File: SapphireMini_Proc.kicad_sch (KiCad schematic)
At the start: 38 parts, among them J801 USB_B_Micro, J802 Conn_02x05_Odd_Even, J803 Conn_02x05_Odd_Even, J805 Conn_01x04_Male, SW701 EVQP7C01P, SW801 EVQP7C01P, U801 ATSAMD21G18A-A

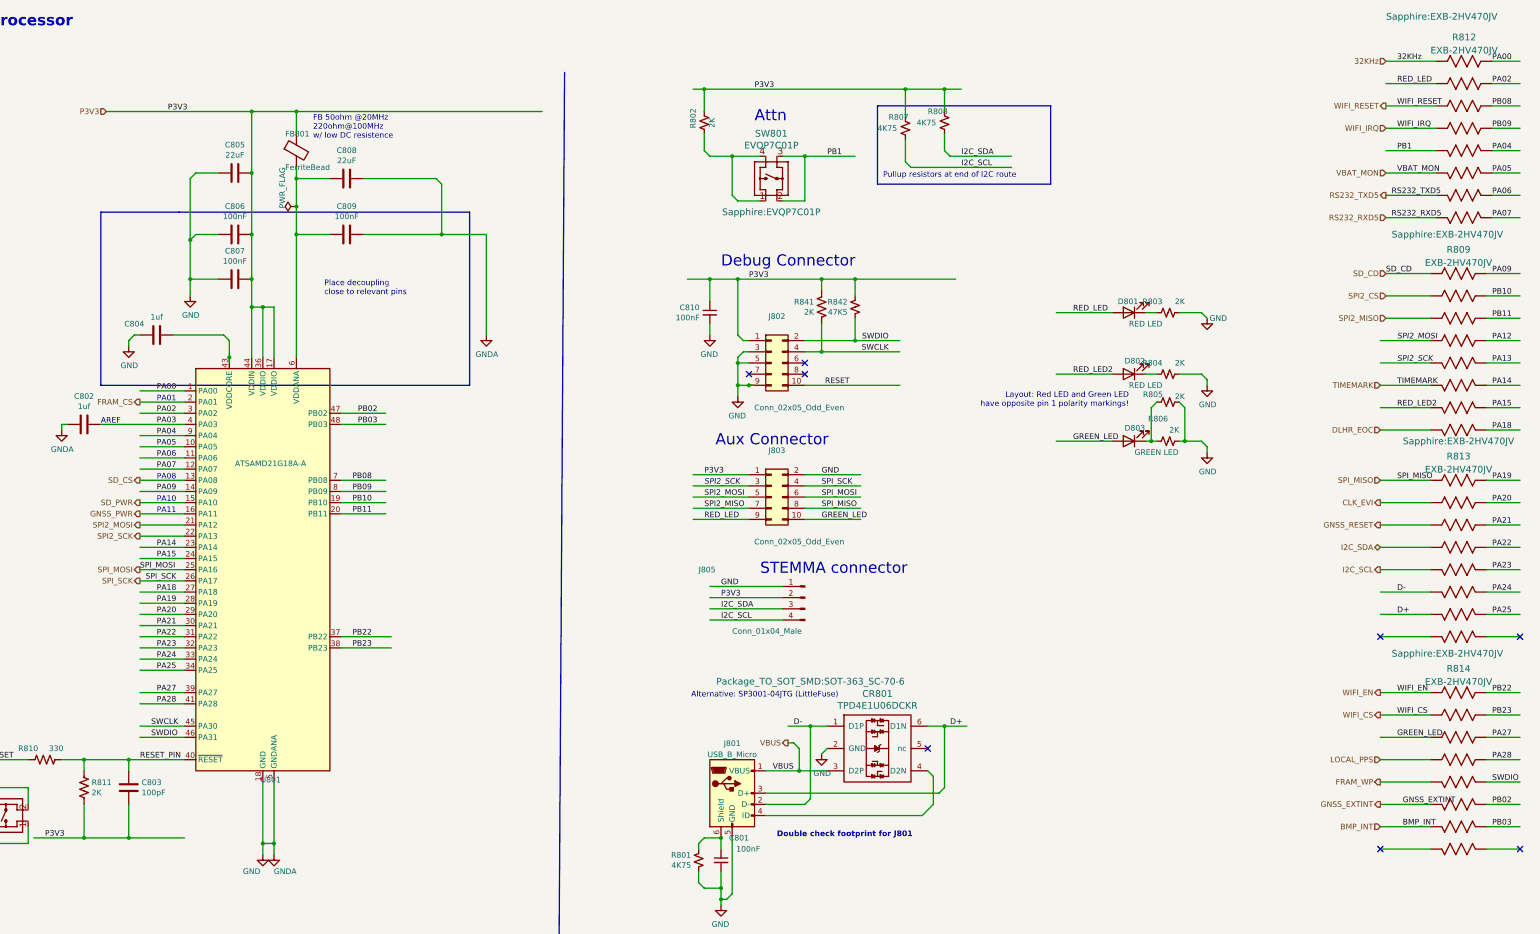
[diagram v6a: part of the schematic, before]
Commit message: 6 Layer Routing
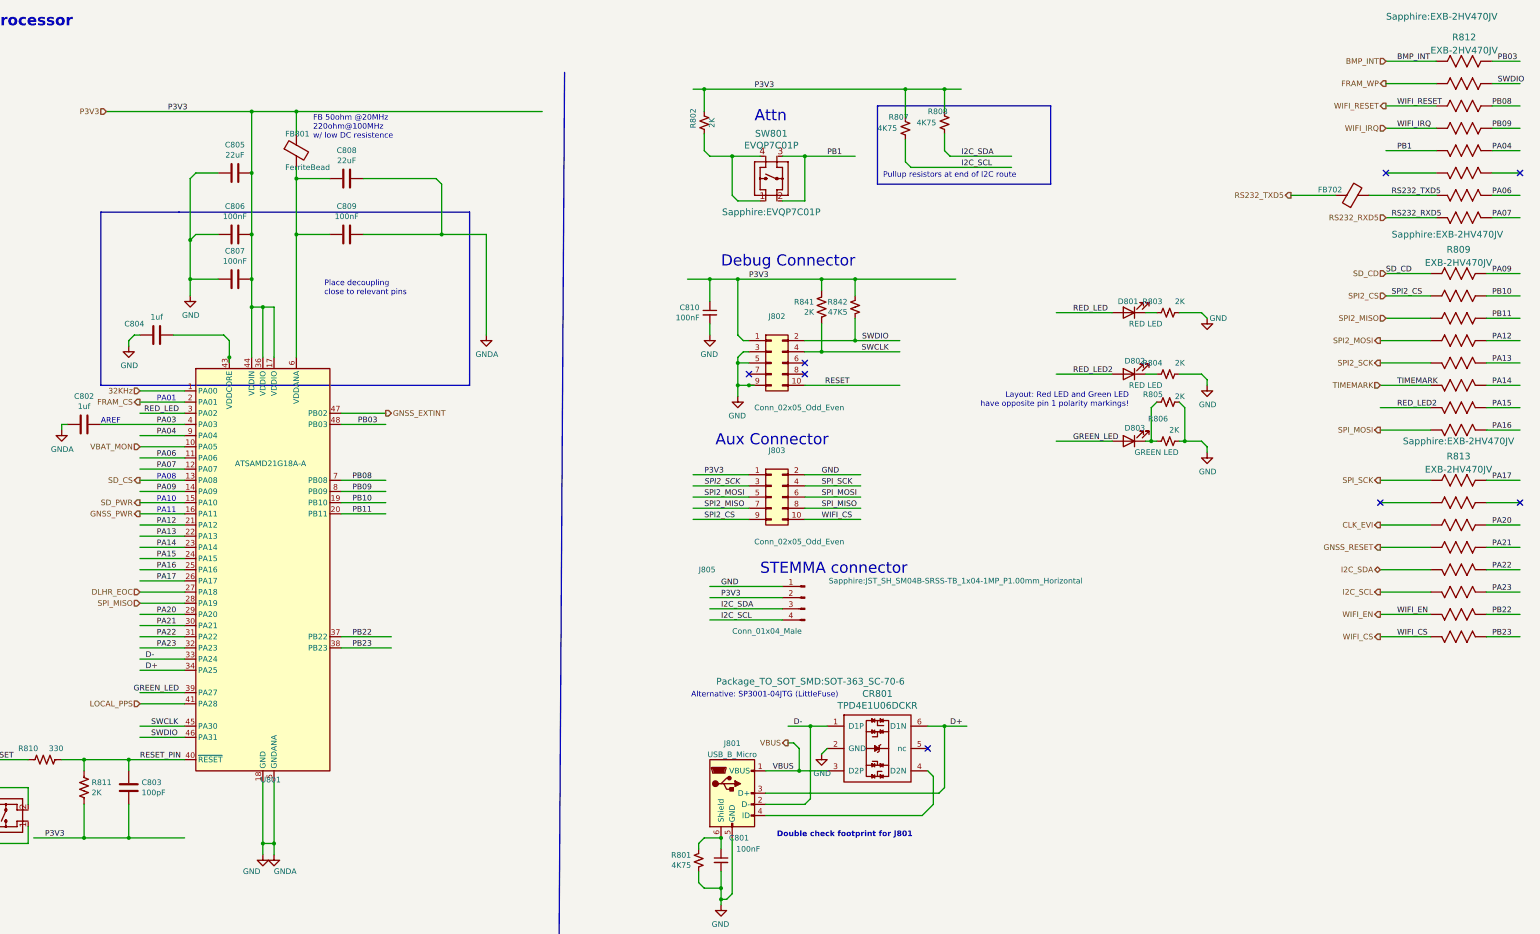
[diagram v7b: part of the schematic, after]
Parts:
- removed R814: EXB-2HV470JV, Sapphire:EXB-2HV470JV, symbol sapphireMini:EXB-2HV470JV_1
- added FB702: FerriteBead, Inductor_SMD:L_0603_1608Metric, symbol Device:FerriteBead
- FB801: footprint Inductor_SMD:L_0201_0603Metric -> Inductor_SMD:L_0603_1608Metric
- J805: footprint Connector_JST:JST_SH_SM04B-SRSS-TB_1x04-1MP_P1.00mm_Horizontal -> Sapphire:JST_SH_SM04B-SRSS-TB_1x04-1MP_P1.00mm_Horizontal; symbol Connector:Conn_01x04_Male -> sapphireMini:Conn_01x04_Male
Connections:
- net PA27 is gone; now on net GREEN_LED: U801.39 (PA27)
- net PA28 is gone; now on net LOCAL_PPS: U801.41 (PA28)
- net PB02 is gone; now on net GNSS_EXTINT: U801.47 (PB02)
- net 32KHz: now also U801.1 (PA00); no longer R812.1
- net BMP_INT: now also R812.1
- net CLK_EVI: now also R813.3; no longer R813.2
- net D+: now also U801.34 (PA25); no longer R813.7
- net D-: now also U801.33 (PA24); no longer R813.6
- net DLHR_EOC: now also U801.27 (PA18); no longer R809.8
- net FRAM_WP: now also R812.2
- net GNSS_RESET: now also R813.4; no longer R813.3
- net GREEN_LED: no longer J803.10 (Pin_10)
- net I2C_SCL: now also R813.6; no longer R813.5
- net I2C_SDA: now also R813.5; no longer R813.4
- net PA12: now also U801.21 (PA12)
- net PA13: now also U801.22 (PA13)
- net PA20: now also R813.14; no longer R813.15
- net PA21: now also R813.13; no longer R813.14
- net PA22: now also R813.12; no longer R813.13
- net PA23: now also R813.11; no longer R813.12
- net PB03: now also R812.16
- net PB22: now also R813.10
- net PB23: now also R813.9
- net RED_LED: now also U801.3 (PA02); no longer J803.9 (Pin_9), R812.2
- net RS232_TXD5: now also FB702.1, FB702.2
- net SPI2_CS: now also J803.9 (Pin_9)
- net SPI2_MOSI: no longer U801.21 (PA12)
- net SPI2_SCK: no longer U801.22 (PA13)
- net SPI_MISO: now also U801.28 (PA19); no longer R813.1
- net SPI_MOSI: now also R809.8; no longer U801.25 (PA16)
- net SPI_SCK: now also R813.1; no longer U801.26 (PA17)
- net SWDIO: now also R812.15
- net VBAT_MON: now also U801.10 (PA05); no longer R812.6
- net WIFI_CS: now also J803.10 (Pin_10), R813.8
- net WIFI_EN: now also R813.7
- removed net PA00: R812.16, U801.1 (PA00)
- removed net PA02: R812.15, U801.3 (PA02)
- net PA05: no longer names the net of R812.11
- net PA05: no longer U801.10 (PA05)
- net PA18 renamed PA16
- net PA16: now also U801.25 (PA16); no longer U801.27 (PA18)
- net PA19 renamed PA17
- net PA17: now also U801.26 (PA17); no longer U801.28 (PA19)
- removed net PA24: R813.11, U801.33 (PA24)
- removed net PA25: R813.10, U801.34 (PA25)

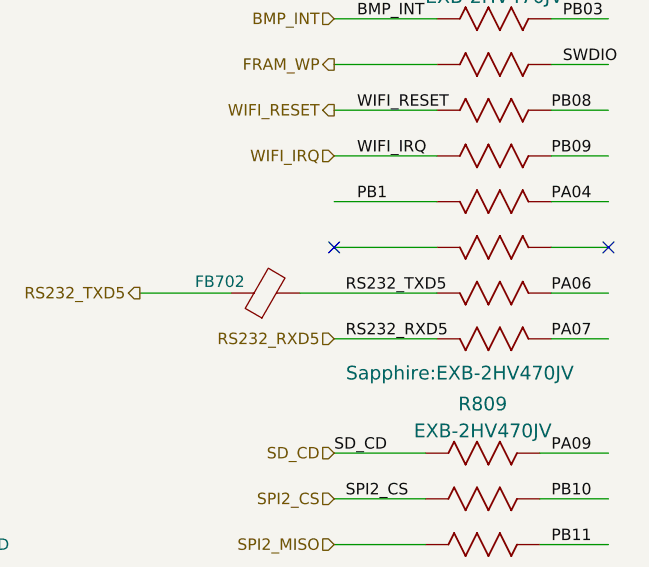
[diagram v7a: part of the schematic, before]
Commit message: 6 Layer Routing
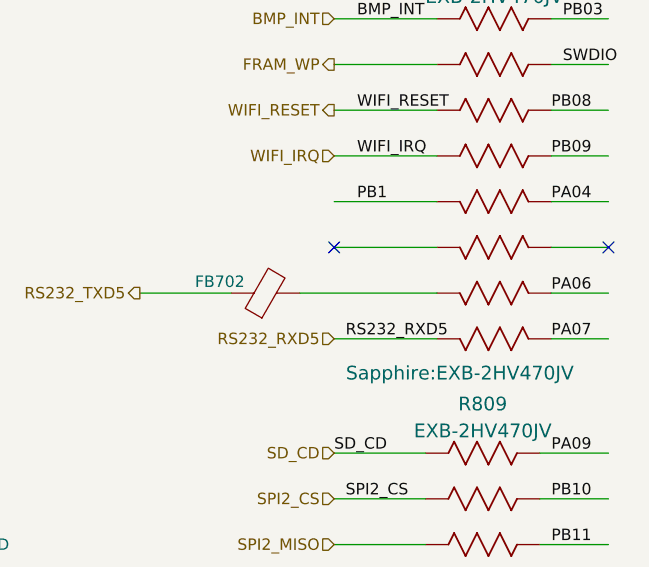
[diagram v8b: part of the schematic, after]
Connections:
- net RS232_TXD5: no longer FB702.2, R812.7
- new net: FB702.2, R812.7
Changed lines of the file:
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@@
-    (effects (font (size 1.27 1.27)) (justify left bottom))
-  )
-  (label "RS232_TXD5" (at 346.71 62.23 0)
     (effects (font (size 1.27 1.27)) (justify left bottom))
   )
